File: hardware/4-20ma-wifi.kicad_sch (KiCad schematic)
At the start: 37 parts, among them J1 Conn_01x19_Female, J2 Conn_01x19_Female, J3 Screw_Terminal_01x02, J4 Screw_Terminal_01x02, J5 Screw_Terminal_01x02, J6 Screw_Terminal_01x02, K1 G5V-1, K2 G5V-1, M1 DC-DC_Buck_Step_Module-dc-dc_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, Q1 2N7002E, Q2 2N7002E, SW1 SW_DIP_x01, U1 ESP32-DEVKITC-32U, U2 LMP8640

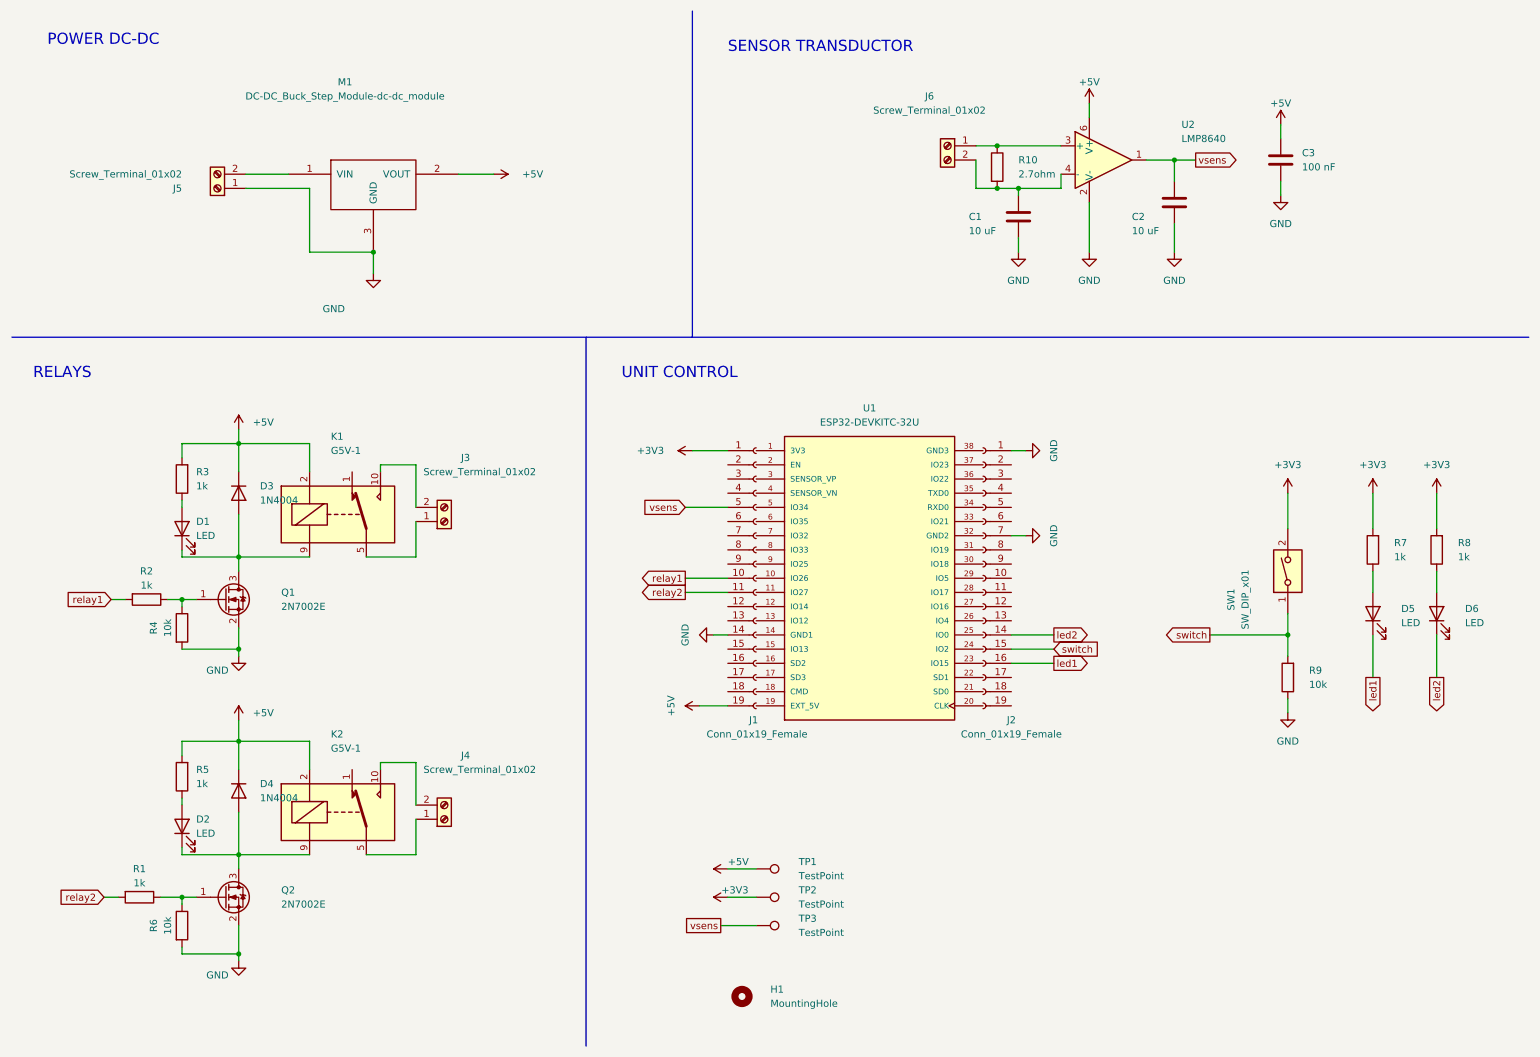
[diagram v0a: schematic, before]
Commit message: Work around PCB design. Added ADC121 to the schematic
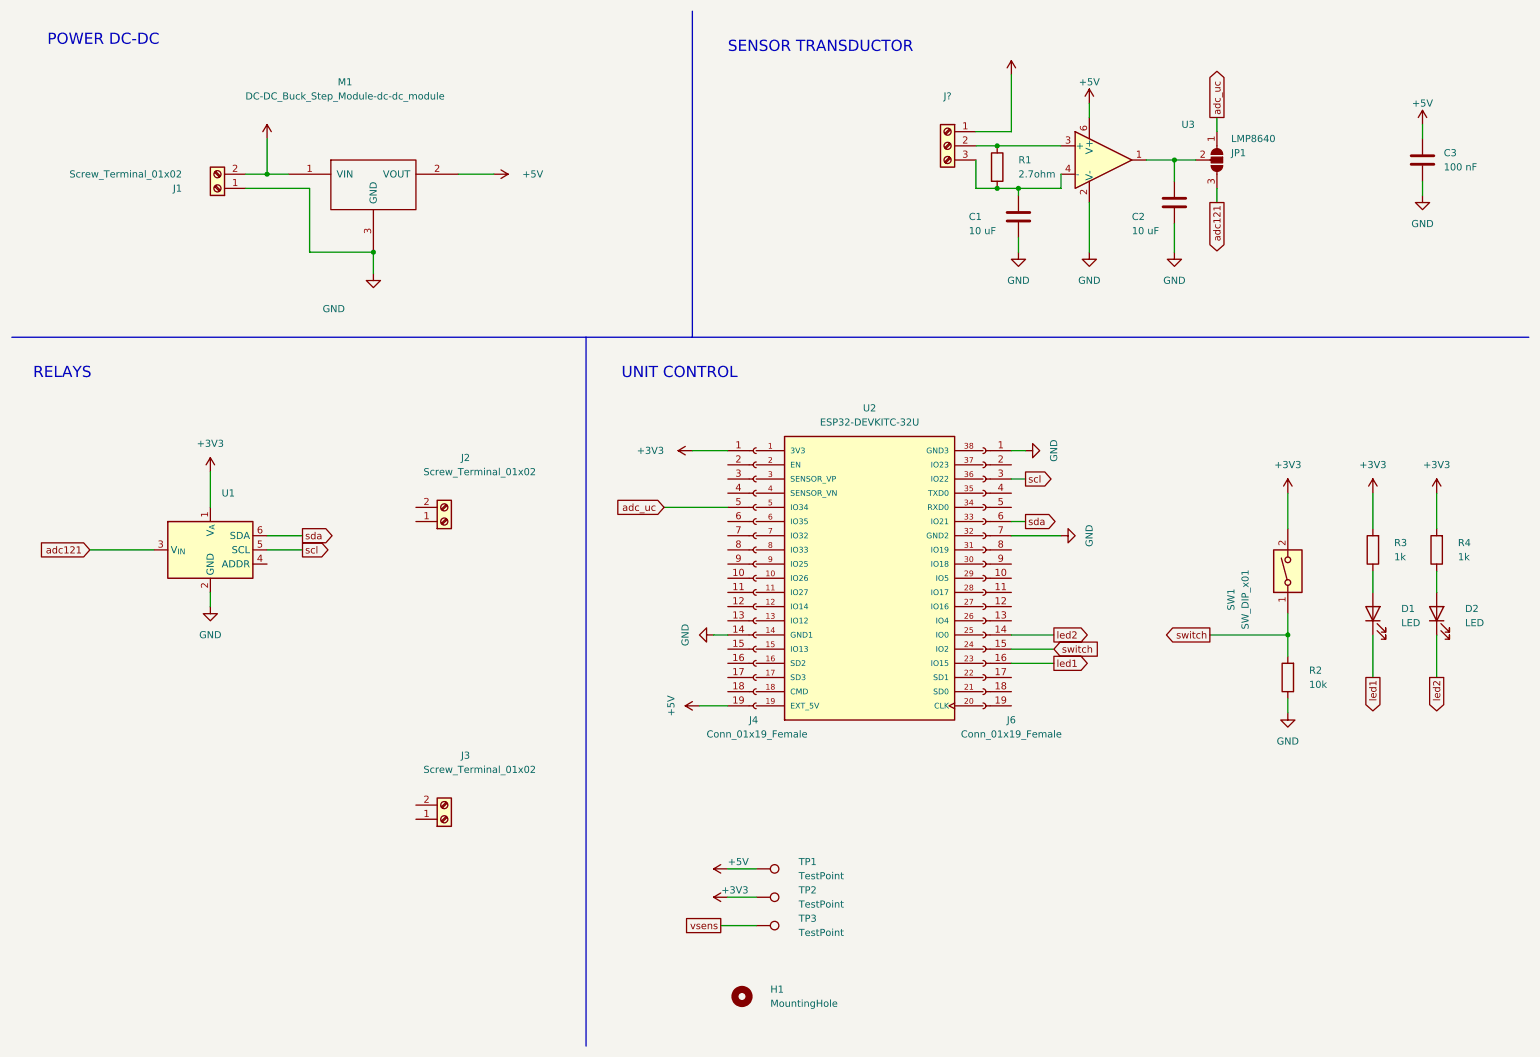
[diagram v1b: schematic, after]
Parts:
- removed D1, D2: LED, LED_THT:LED_D3.0mm_FlatTop, symbol Device:LED
- removed D3, D4: 1N4004, Diode_SMD:D_SMA, symbol Diode:1N4004
- removed J6: Screw_Terminal_01x02, project_library:TerminalBlock__1x02_P5.00mm_90Degree, symbol Connector:Screw_Terminal_01x02
- removed K1, K2: G5V-1, Relay_THT:Relay_SPDT_Omron_G5V-1, symbol Relay:G5V-1
- removed Q1, Q2: 2N7002E, Package_TO_SOT_SMD:SOT-23, symbol Transistor_FET:2N7002E
- removed R1, R2, R3, R5: 1k, Resistor_SMD:R_0805_2012Metric_Pad1.20x1.40mm_HandSolder, symbol Device:R
- removed R4, R6: 10k, Resistor_SMD:R_0805_2012Metric_Pad1.20x1.40mm_HandSolder, symbol Device:R
- added J?: (no value), symbol Connector:Screw_Terminal_01x03
- added JP1: (no value), symbol Jumper:SolderJumper_3_Open
- added U1: (no value), symbol Analog_ADC:ADC101C021CIMK
- renumbered D5 to D1, D6 to D2, J5 to J1, J3 to J2, J4 to J3, J1 to J4, J2 to J6, R10 to R1, R9 to R2, R7 to R3, R8 to R4, U1 to U2, U2 to U3
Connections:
- net +3V3: now also U1.1 (V_{A})
- net GND: now also U1.2 (GND)
- net vsens: no longer C2.1, J4.5 (Pin_5), U3.1
- net +12V: now reaches J1.2 (Pin_2), M1.1 (VIN)
- net +12V: now also J?.1 (Pin_1)
- net at R1.1, U3.3 (+): now also J?.2 (Pin_2)
- net at C1.1, R1.2, U3.4 (-): now also J?.3 (Pin_3)
- net scl: now reaches J6.3 (Pin_3)
- net scl: now also U1.5 (SCL)
- net sda: now reaches J6.6 (Pin_6)
- net sda: now also U1.6 (SDA)
- net relay1: no longer names the net of J4.10 (Pin_10)
- net relay2: no longer names the net of J4.11 (Pin_11)
- new net: C2.1, JP1.2 (C), U3.1
- new net adc121: JP1.3 (B), U1.3 (V_{IN})
- new net adc_uc: J4.5 (Pin_5), JP1.1 (A)
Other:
- moved on the sheet: C3

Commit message: Work around PCB design
- Added new terminal block to connect usar or i2c device
- Added shift-level to 3.3 - 5v usart/i2c
- Work around layout
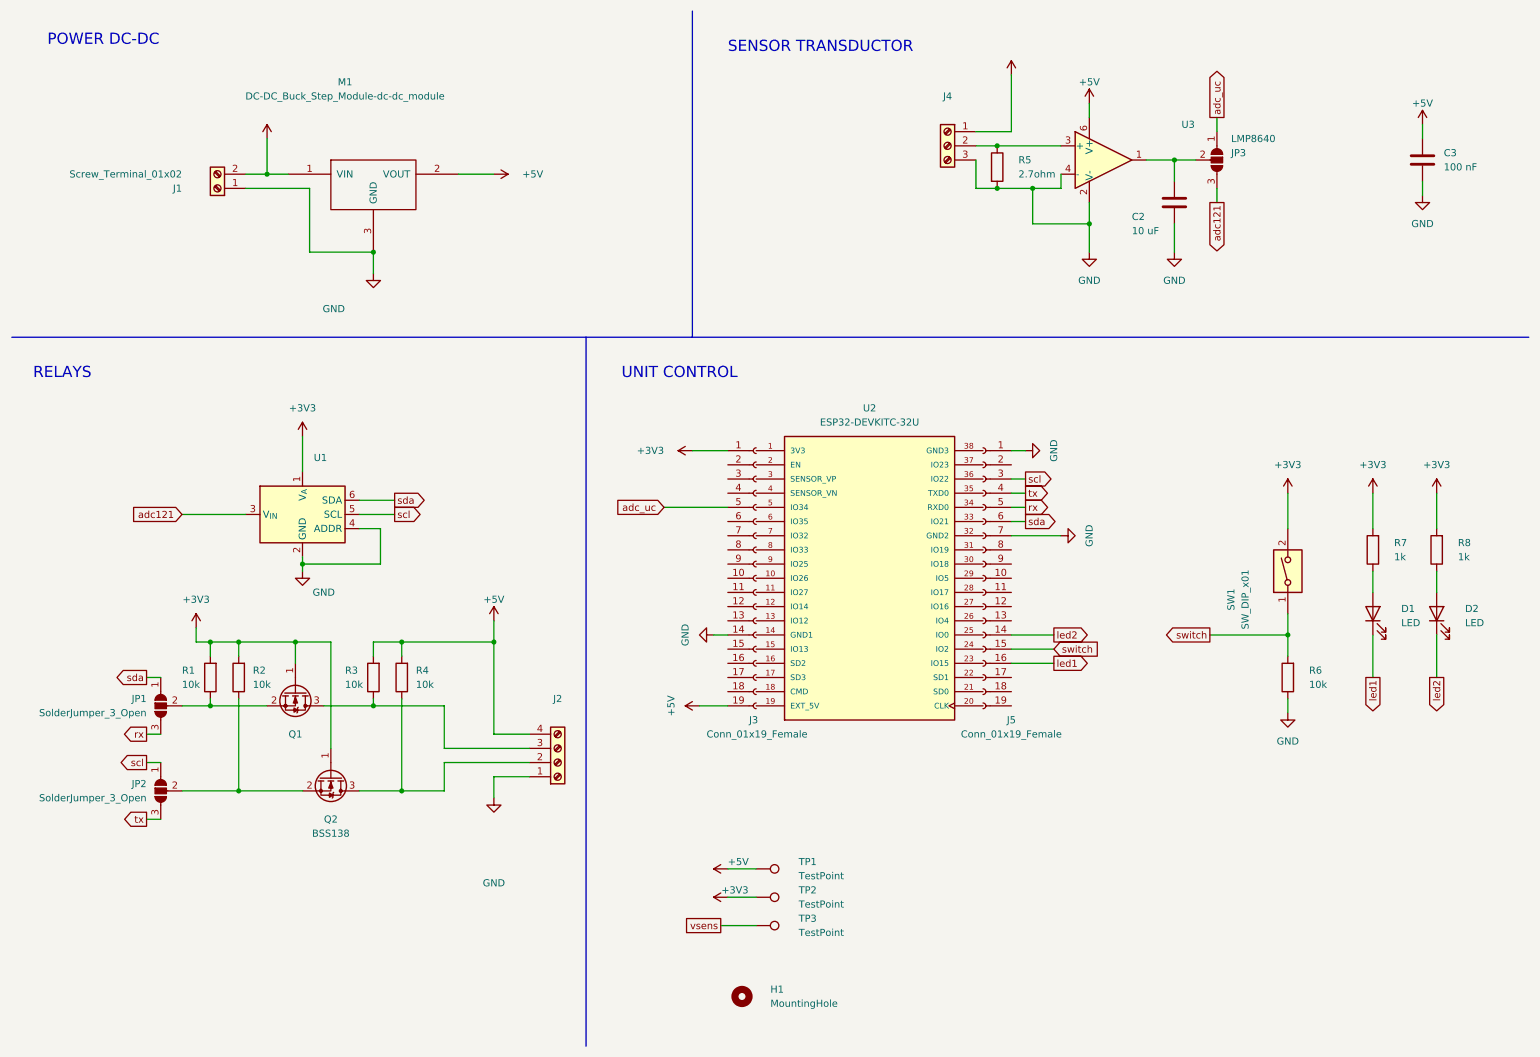
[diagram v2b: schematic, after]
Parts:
- removed C1: 10 uF, Capacitor_SMD:C_0805_2012Metric_Pad1.18x1.45mm_HandSolder, symbol Device:C
- removed J2, J3: Screw_Terminal_01x02, project_library:TerminalBlock__1x02_P5.00mm_90Degree, symbol Connector:Screw_Terminal_01x02
- added J2: (no value), symbol Connector:Screw_Terminal_01x04
- added JP1, JP2: SolderJumper_3_Open, Jumper:SolderJumper-3_P1.3mm_Open_RoundedPad1.0x1.5mm, symbol Jumper:SolderJumper_3_Open
- added Q1: (no value), symbol Transistor_FET:BSS138
- added Q2: BSS138, Package_TO_SOT_SMD:SOT-23, symbol Transistor_FET:BSS138
- added R1, R2, R3, R4: 10k, Resistor_SMD:R_0805_2012Metric_Pad1.20x1.40mm_HandSolder, symbol Device:R
- gave numbers to parts that had none: 1
- renumbered J4 to J3, J6 to J5, JP1 to JP3, R1 to R5, R2 to R6, R3 to R7, R4 to R8
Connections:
- net +3V3: now also Q1.1 (G), Q2.1 (G), R1.2, R2.2
- net +5V: now also J2.4 (Pin_4), R3.2, R4.2
- net GND: now also J4.3 (Pin_3), R5.2, U1.4 (ADDR), U3.4 (-), J2.1 (Pin_1)
- net scl: now also JP2.1 (A)
- net sda: now also JP1.1 (A)
- net tx: now reaches J5.4 (Pin_4)
- net tx: now also JP2.3 (B)
- net rx: now reaches J5.5 (Pin_5)
- net rx: now also JP1.3 (B)
- new net: JP1.2 (C), Q1.2 (S), R1.1
- new net: J2.3 (Pin_3), Q1.3 (D), R3.1
- new net: J2.2 (Pin_2), Q2.3 (D), R4.1
- new net: JP2.2 (C), Q2.2 (S), R2.1
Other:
- moved on the sheet: U1

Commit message: Work around pcb layout
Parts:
- removed TP3: TestPoint, TestPoint:TestPoint_Pad_D1.0mm, symbol Connector:TestPoint
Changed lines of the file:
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@@
-    (stroke (width 0) (type default) (color 0 0 0 0))
-  )
-  (wire (pts (xy 139.7 176.53) (xy 146.05 176.53))
     (stroke (width 0) (type default) (color 0 0 0 0))
   )
@@
     (effects (font (size 1.27 1.27)) (justify right))
     (property "Intersheet References" "${INTERSHEET_REFS}" (id 0) (at 267.8906 138.6055 90)
-      (effects (font (size 1.27 1.27)) (justify right) hide)
-    )
-  )
-  (global_label "vsens" (shape passive) (at 139.7 176.53 180) (fields_autoplaced)
-    (effects (font (size 1.27 1.27)) (justify right))
-    (property "Intersheet References" "${INTERSHEET_REFS}" (id 0) (at 132.0255 176.4506 0)
       (effects (font (size 1.27 1.27)) (justify right) hide)
     )
@@
     )
     (property "Datasheet" "" (id 3) (at 241.3 138.43 0)
-      (effects (font (size 1.27 1.27)) hide)
-    )
-    (pin "1")
-  )
-  (symbol (lib_id "Connector:TestPoint") (at 146.05 176.53 270) (unit 1)
-    (in_bom yes) (on_board yes) (fields_autoplaced)
-    (property "Reference" "TP3" (id 0) (at 153.67 175.2599 90)
-      (effects (font (size 1.27 1.27)) (justify left))
-    )
-    (property "Value" "TestPoint" (id 1) (at 153.67 177.7999 90)
-      (effects (font (size 1.27 1.27)) (justify left))
-    )
-    (property "Footprint" "TestPoint:TestPoint_Pad_D1.0mm" (id 2) (at 146.05 181.61 0)
-      (effects (font (size 1.27 1.27)) hide)
-    )
-    (property "Datasheet" "~" (id 3) (at 146.05 181.61 0)
       (effects (font (size 1.27 1.27)) hide)
     )
@@
       (reference "TP2") (unit 1) (value "TestPoint") (footprint "TestPoint:TestPoint_Pad_D1.0mm")
     )
-    (path "/6aaf68cd-0b1f-4133-ab14-943877d783dc"
-      (reference "TP3") (unit 1) (value "TestPoint") (footprint "TestPoint:TestPoint_Pad_D1.0mm")
-    )
     (path "/131591c0-0ebb-44a4-b02e-592ed1debb2d"

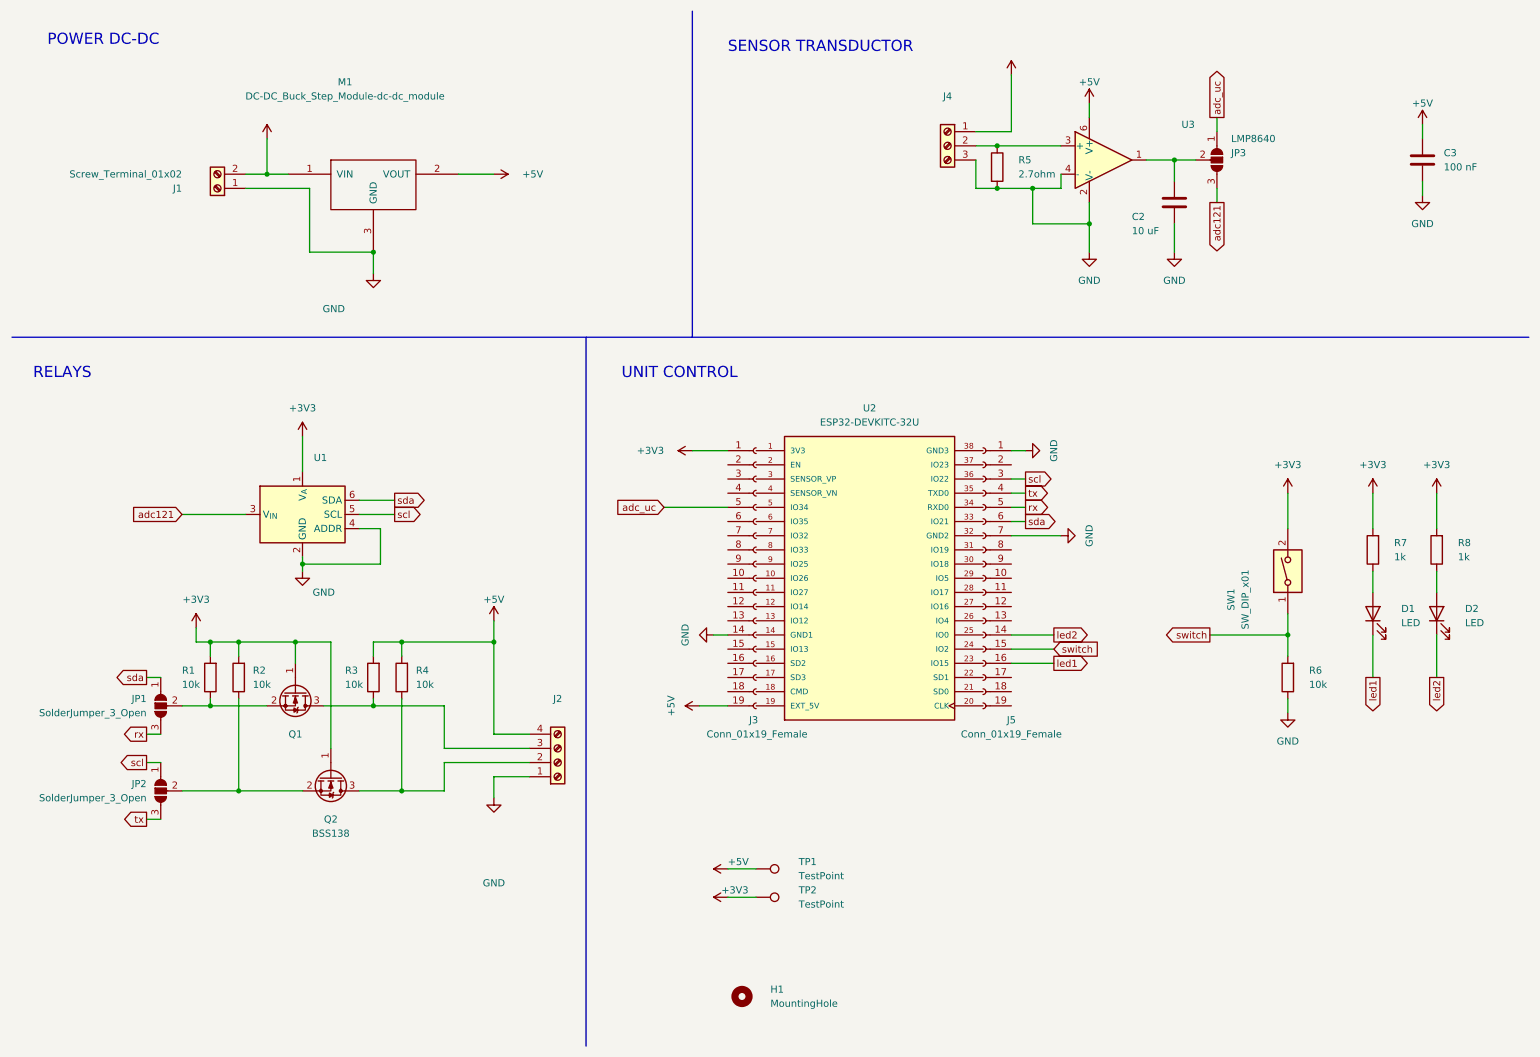
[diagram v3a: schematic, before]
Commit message: Added LP2980 Dropout regulator to power the ADC converter
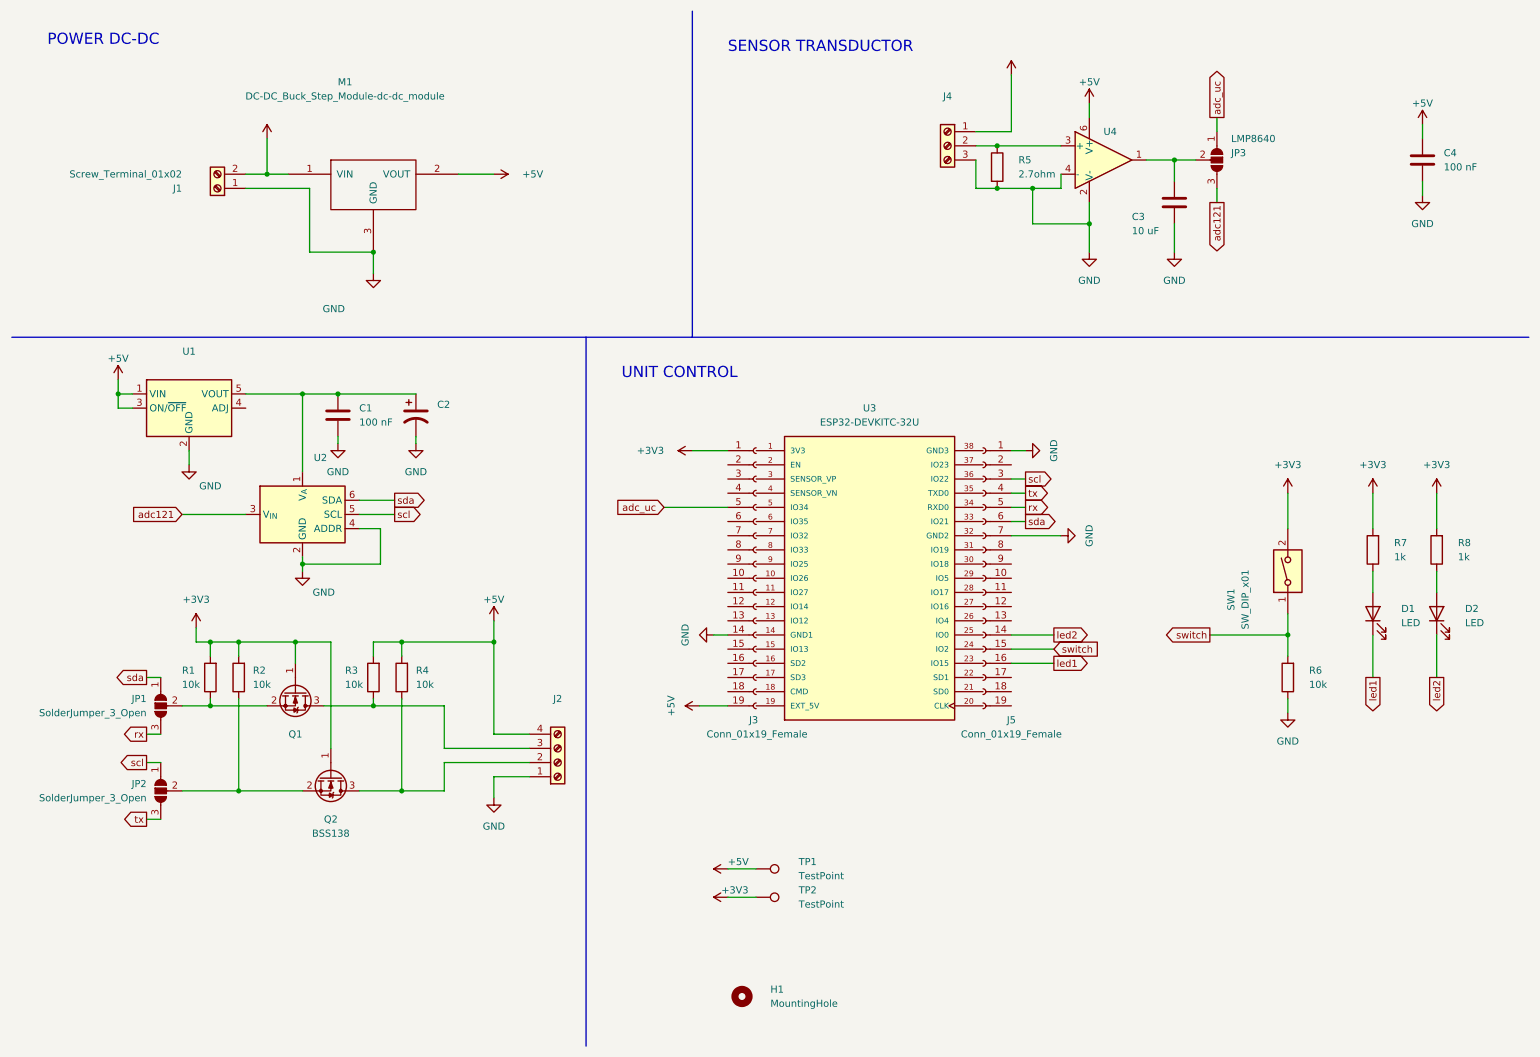
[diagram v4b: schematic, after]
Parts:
- added C1: 100 nF, Capacitor_SMD:C_0805_2012Metric_Pad1.18x1.45mm_HandSolder, symbol Device:C
- added C2: (no value), symbol Device:C_Polarized_US
- added U1: (no value), symbol Regulator_Linear:LP2980-ADJ
- renumbered C2 to C3, C3 to C4, U1 to U2, U2 to U3, U3 to U4
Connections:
- net +3V3: no longer U2.1 (V_{A})
- net +5V: now also U1.1 (VIN), U1.3 (ON/~{OFF})
- net GND: now also C1.2, C2.2, U1.2 (GND)
- new net: C1.1, C2.1, U1.5 (VOUT), U2.1 (V_{A})
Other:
- note removed: "RELAYS"
